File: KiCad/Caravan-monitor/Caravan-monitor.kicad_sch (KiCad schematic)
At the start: 24 parts, among them J1 Conn_ARM_JTAG_SWD_20, J2 8-28V input, SW2 SW_USER, SW3 SW_DPDT_x2, U2 STM32L010C6Tx

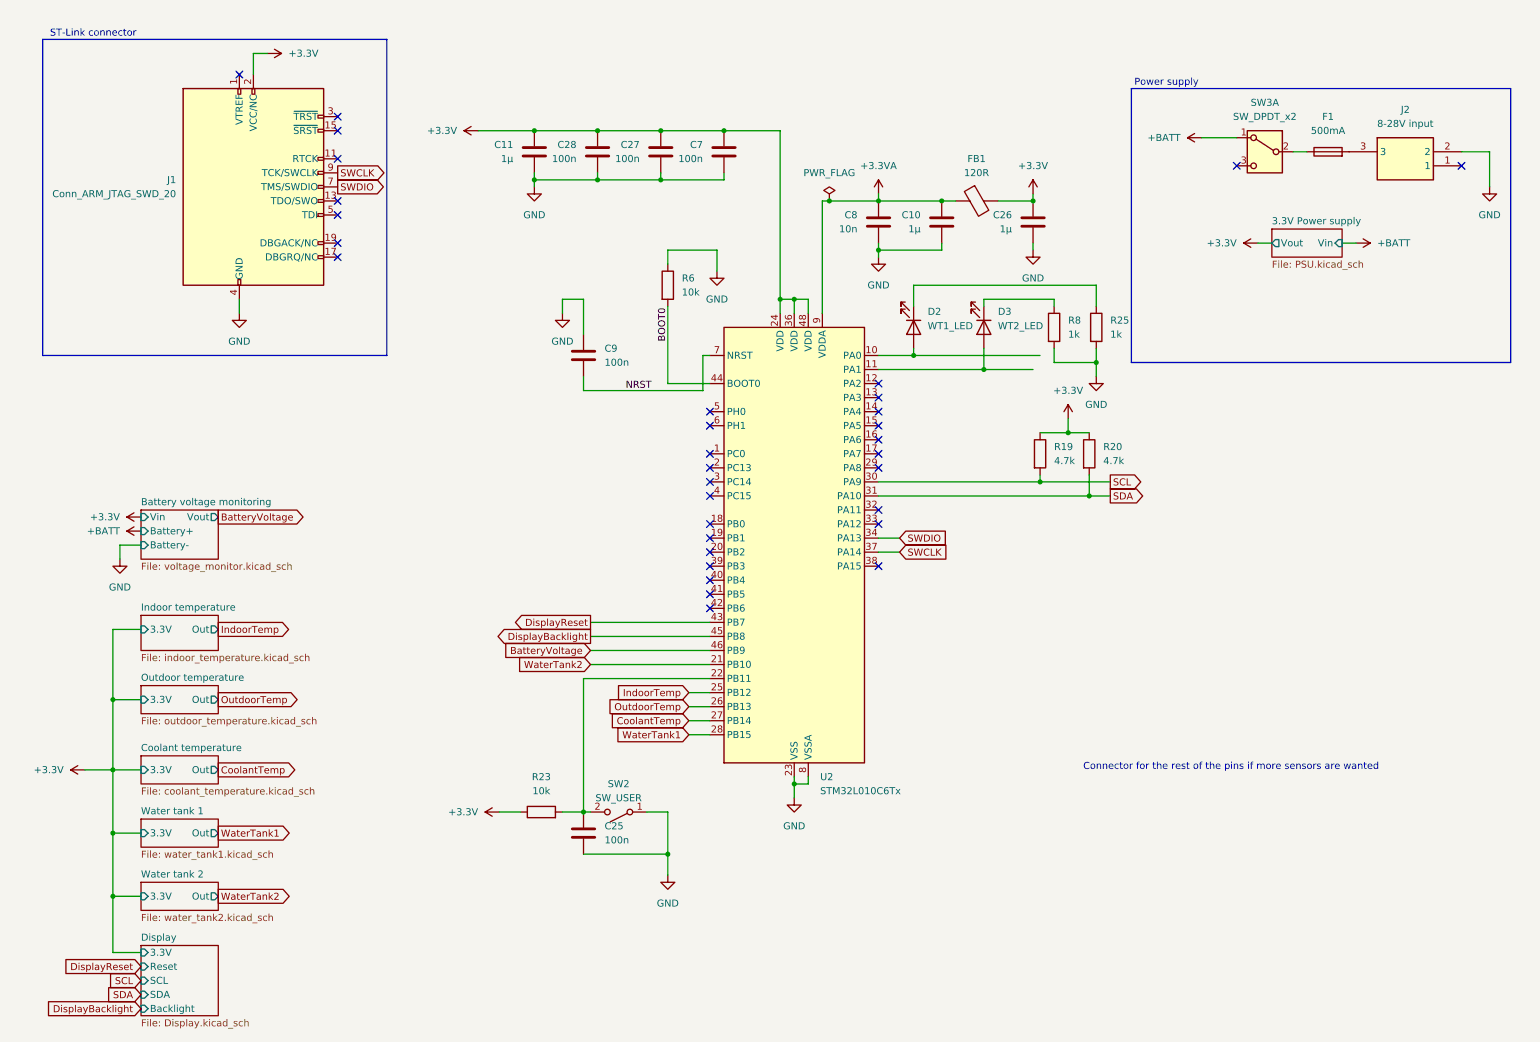
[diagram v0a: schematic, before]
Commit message: Schematic updates
Parts changed for JLCPCB assembly compatibility
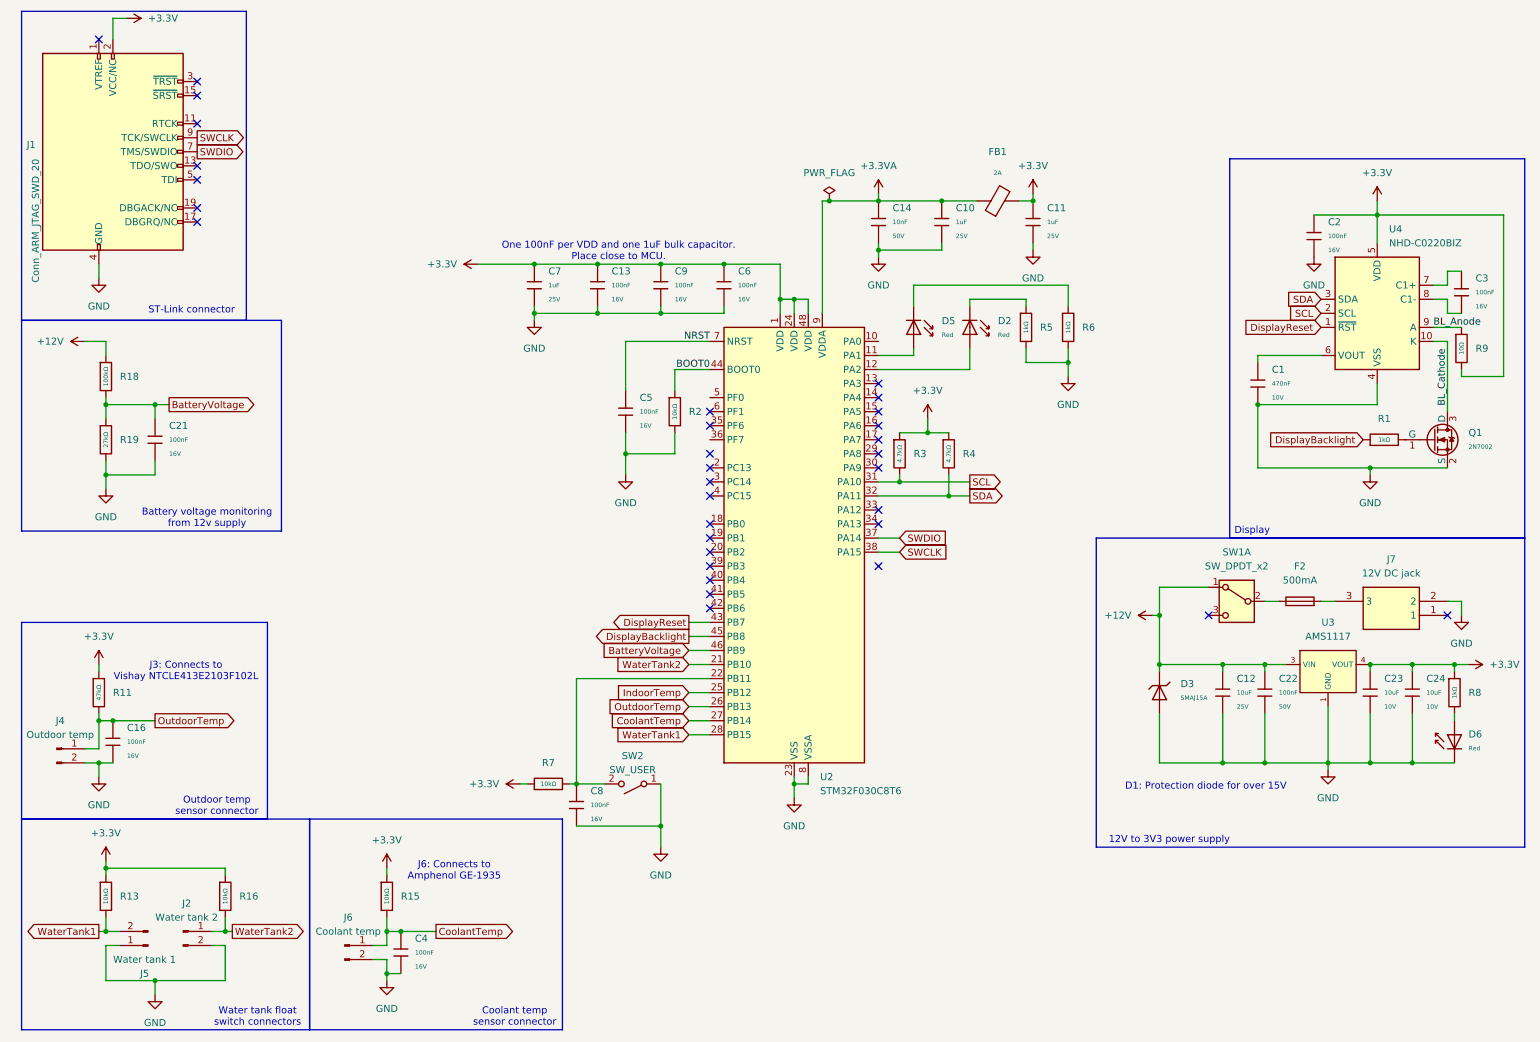
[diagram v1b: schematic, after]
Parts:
- removed C10, C11, C26: 1µ, Capacitor_SMD:C_0402_1005Metric_Pad0.74x0.62mm_HandSolder, symbol Device:C
- removed C25, C27, C28, C7, C9: 100n, Capacitor_SMD:C_0402_1005Metric_Pad0.74x0.62mm_HandSolder, symbol Device:C
- removed C8: 10n, Capacitor_SMD:C_0402_1005Metric_Pad0.74x0.62mm_HandSolder, symbol Device:C
- removed D2: WT1_LED, LED_SMD:LED_0402_1005Metric_Pad0.77x0.64mm_HandSolder, symbol Device:LED
- removed D3: WT2_LED, LED_SMD:LED_0402_1005Metric_Pad0.77x0.64mm_HandSolder, symbol Device:LED
- removed F1: 500mA, Fuse:Fuseholder_Clip-5x20mm_Littelfuse_111_Lateral_P18.80x5.00mm_D1.17mm_Horizontal, symbol Device:Fuse
- removed FB1: 120R, Inductor_SMD:L_0402_1005Metric_Pad0.77x0.64mm_HandSolder, symbol Device:FerriteBead
- removed J2: 8-28V input, SamacSys_Parts:PJ059A, symbol SamacSys_Parts:PJ-059A
- removed R19, R20: 4.7k, Resistor_SMD:R_0402_1005Metric_Pad0.72x0.64mm_HandSolder, symbol Device:R
- removed R23, R6: 10k, Resistor_SMD:R_0402_1005Metric_Pad0.72x0.64mm_HandSolder, symbol Device:R
- removed R25, R8: 1k, Resistor_SMD:R_0402_1005Metric_Pad0.72x0.64mm_HandSolder, symbol Device:R
- removed SW3: SW_DPDT_x2, Button_Switch_THT:SW_E-Switch_EG2219_DPDT_Angled, symbol Switch:SW_DPDT_x2
- removed U2: STM32L010C6Tx, Package_QFP:LQFP-48_7x7mm_P0.5mm, symbol MCU_ST_STM32L0:STM32L010C6Tx
- added C1: 470nF, PCM_JLCPCB:C_0402, symbol PCM_JLCPCB-Capacitors:0402,470nF
- added C10, C11, C7: 1uF, PCM_JLCPCB:C_0402, symbol PCM_JLCPCB-Capacitors:0402,1uF
- added C12: 10uF, PCM_JLCPCB:C_0805, symbol PCM_JLCPCB-Capacitors:0805,10uF
- added C13, C16, C2, C21, C3, C4, C5, C6, C8, C9: 100nF, PCM_JLCPCB:C_0402, symbol PCM_JLCPCB-Capacitors:0402,100nF
- added C14: 10nF, PCM_JLCPCB:C_0402, symbol PCM_JLCPCB-Capacitors:0402,10nF
- added C22: 100nF, PCM_JLCPCB:C_0603, symbol PCM_JLCPCB-Capacitors:0603,100nF
- added C23, C24: 10uF, PCM_JLCPCB:C_0603, symbol PCM_JLCPCB-Capacitors:0603,10uF
- added D2, D5, D6: Red, PCM_JLCPCB:D_0603, symbol PCM_JLCPCB-Diodes:LED,0603,Red
- added D3: SMAJ15A, PCM_JLCPCB:D_SMA, symbol PCM_JLCPCB-Diodes:TVS-Uni,SMAJ15A
- added F2: 500mA, Fuse:Fuseholder_Clip-5x20mm_Littelfuse_111_Lateral_P18.80x5.00mm_D1.17mm_Horizontal, symbol Device:Fuse
- added FB1: ~, PCM_JLCPCB:FB_0603, symbol PCM_JLCPCB-Inductors:Ferrite,0603,(2)
- added J2: Water tank 2, Connector_JST:JST_XH_S2B-XH-A-1_1x02_P2.50mm_Horizontal, symbol Connector:Conn_01x02_Pin
- added J4: Outdoor temp, Connector_JST:JST_XH_S2B-XH-A-1_1x02_P2.50mm_Horizontal, symbol Connector:Conn_01x02_Pin
- added J5: Water tank 1, Connector_JST:JST_XH_S2B-XH-A-1_1x02_P2.50mm_Horizontal, symbol Connector:Conn_01x02_Pin
- added J6: Coolant temp, Connector_JST:JST_XH_S2B-XH-A-1_1x02_P2.50mm_Horizontal, symbol Connector:Conn_01x02_Pin
- added J7: 12V DC jack, SamacSys_Parts:PJ059A, symbol SamacSys_Parts:PJ-059A
- added Q1: 2N7002, PCM_JLCPCB:Q_SOT-23, symbol PCM_JLCPCB-Transistors:NMOS,2N7002
- added R1, R5, R6, R8: 1kΩ, PCM_JLCPCB:R_0402, symbol PCM_JLCPCB-Resistors:0402,1kΩ
- added R11: 47kΩ, PCM_JLCPCB:R_0402, symbol PCM_JLCPCB-Resistors:0402,47kΩ
- added R13, R15, R16, R2, R7: 10kΩ, PCM_JLCPCB:R_0402, symbol PCM_JLCPCB-Resistors:0402,10kΩ
- added R18: 100kΩ, PCM_JLCPCB:R_0402, symbol PCM_JLCPCB-Resistors:0402,100kΩ
- added R19: 27kΩ, PCM_JLCPCB:R_0402, symbol PCM_JLCPCB-Resistors:0402,27kΩ
- added R3, R4: 4.7kΩ, PCM_JLCPCB:R_0402, symbol PCM_JLCPCB-Resistors:0402,4.7kΩ
- added R9: 10Ω, PCM_JLCPCB:R_0603, symbol PCM_JLCPCB-Resistors:0603,10Ω
- added SW1: SW_DPDT_x2, Button_Switch_THT:SW_E-Switch_EG2219_DPDT_Angled, symbol Switch:SW_DPDT_x2
- added U2: STM32F030C8T6, PCM_JLCPCB:LQFP-48_7x7mm_P0.5mm, symbol PCM_JLCPCB-MCUs:STM32F030C8T6
- added U3: AMS1117, PCM_JLCPCB:SOT-223-3_L6.5-W3.4-P2.30-LS7.0-BR, symbol PCM_JLCPCB-Power:LDO, 3.3V, 1A
- added U4: NHD-C0220BIZ, Display:NHD-C0220BiZ, symbol Display_Character:NHD-C0220BIZ
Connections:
- net +3.3V: now also C11.1, C13.1, C2.1, C23.1, C24.1, C6.1, C7.1, C9.1, FB1.2, R11.1, R13.1, R15.1, R16.1, R3.1, R4.1, R7.1, R8.1, R9.2, U2.1 (VDD), U2.24 (VDD), U2.48 (VDD), U3.2 (VOUT), U3.4 (VOUT), U4.5 (VDD)
- net +3.3VA: now also C10.1, C14.1, FB1.1, U2.9 (VDDA)
- net BOOT0: now also R2.1, U2.44 (BOOT0)
- net BatteryVoltage: now also C21.1, R18.2, R19.1, U2.46 (PB9)
- net CoolantTemp: now also C4.1, J6.1 (Pin_1), R15.2, U2.27 (PB14)
- net DisplayBacklight: now also R1.1, U2.45 (PB8)
- net DisplayReset: now also U2.43 (PB7), U4.1 (~{RST})
- net GND: now also C1.2, C10.2, C11.2, C12.2, C13.2, C14.2, C16.2, C2.2, C21.2, C22.2, C23.2, C24.2, C4.2, C5.2, C6.2, C7.2, C8.2, C9.2, D3.2, D6.1, J2.2 (Pin_2), J4.2 (Pin_2), J5.1 (Pin_1), J6.2 (Pin_2), J7.2, Q1.2 (S), R19.2, R2.2, R5.2, R6.2, U2.23 (VSS), U2.47 (VSS), U2.8 (VSSA), U3.1 (GND), U4.4 (VSS)
- net IndoorTemp: now also U2.25 (PB12)
- net NRST: now also C5.1, U2.7 (NRST)
- net OutdoorTemp: now also C16.1, J4.1 (Pin_1), R11.2, U2.26 (PB13)
- net SCL: now also R3.2, U2.31 (PA10), U4.2 (SCL)
- net SDA: now also R4.2, U2.32 (PA11), U4.3 (SDA)
- net SWCLK: now also U2.38 (PA15)
- net SWDIO: now also U2.37 (PA14)
- net WaterTank1: now also J5.2 (Pin_2), R13.2, U2.28 (PB15)
- net WaterTank2: now also J2.1 (Pin_1), R16.2, U2.21 (PB10)
- net at SW2.2 (B): now also C8.1, R7.2, U2.22 (PB11)
- new net: F2.1, SW1.2 (B)
- new net: D5.2, U2.11 (PA1)
- new net: D2.2, U2.12 (PA2)
- new net: D2.1, R5.1
- new net: C1.1, U4.6 (VOUT)
- new net: C3.1, U4.7 (C1+)
- new net: C3.2, U4.8 (C1-)
- new net: D5.1, R6.1
- new net: F2.2, J7.3
- new net: Q1.1 (G), R1.2
- new net: D6.2, R8.2
- new net +12V: C12.1, C22.1, D3.1, R18.1, SW1.1 (A), U3.3 (VIN)
- new net BL_Anode: R9.1, U4.9 (A)
- new net BL_Cathode: Q1.3 (D), U4.10 (K)
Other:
- removed sheet 3.3V Power supply
- removed sheet Battery voltage monitoring
- removed sheet Coolant temperature
- removed sheet Display
- removed sheet Indoor temperature
- removed sheet Outdoor temperature
- removed sheet Water tank 1
- removed sheet Water tank 2
- note added: "12V to 3V3 power supply"
- note added: "Battery voltage monitoring from 12v supply"
- note added: "Coolant temp sensor connector"
- note added: "D1: Protection diode for over 15V"
- note added: "Display"
- note added: "J3: Connects to Vishay NTCLE413E2103F102L"
- note added: "J6: Connects to Amphenol GE-1935"
- note added: "One 100nF per VDD and one 1uF bulk capacitor. Place close to MCU."
- note added: "Outdoor temp sensor connector"
- note added: "Water tank float switch connectors"
- note removed: "Connector for the rest of the pins if more sensors are wanted"
- note removed: "Power supply"
- moved on the sheet: J1, SW2

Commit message: 12V to 3.3V converter done
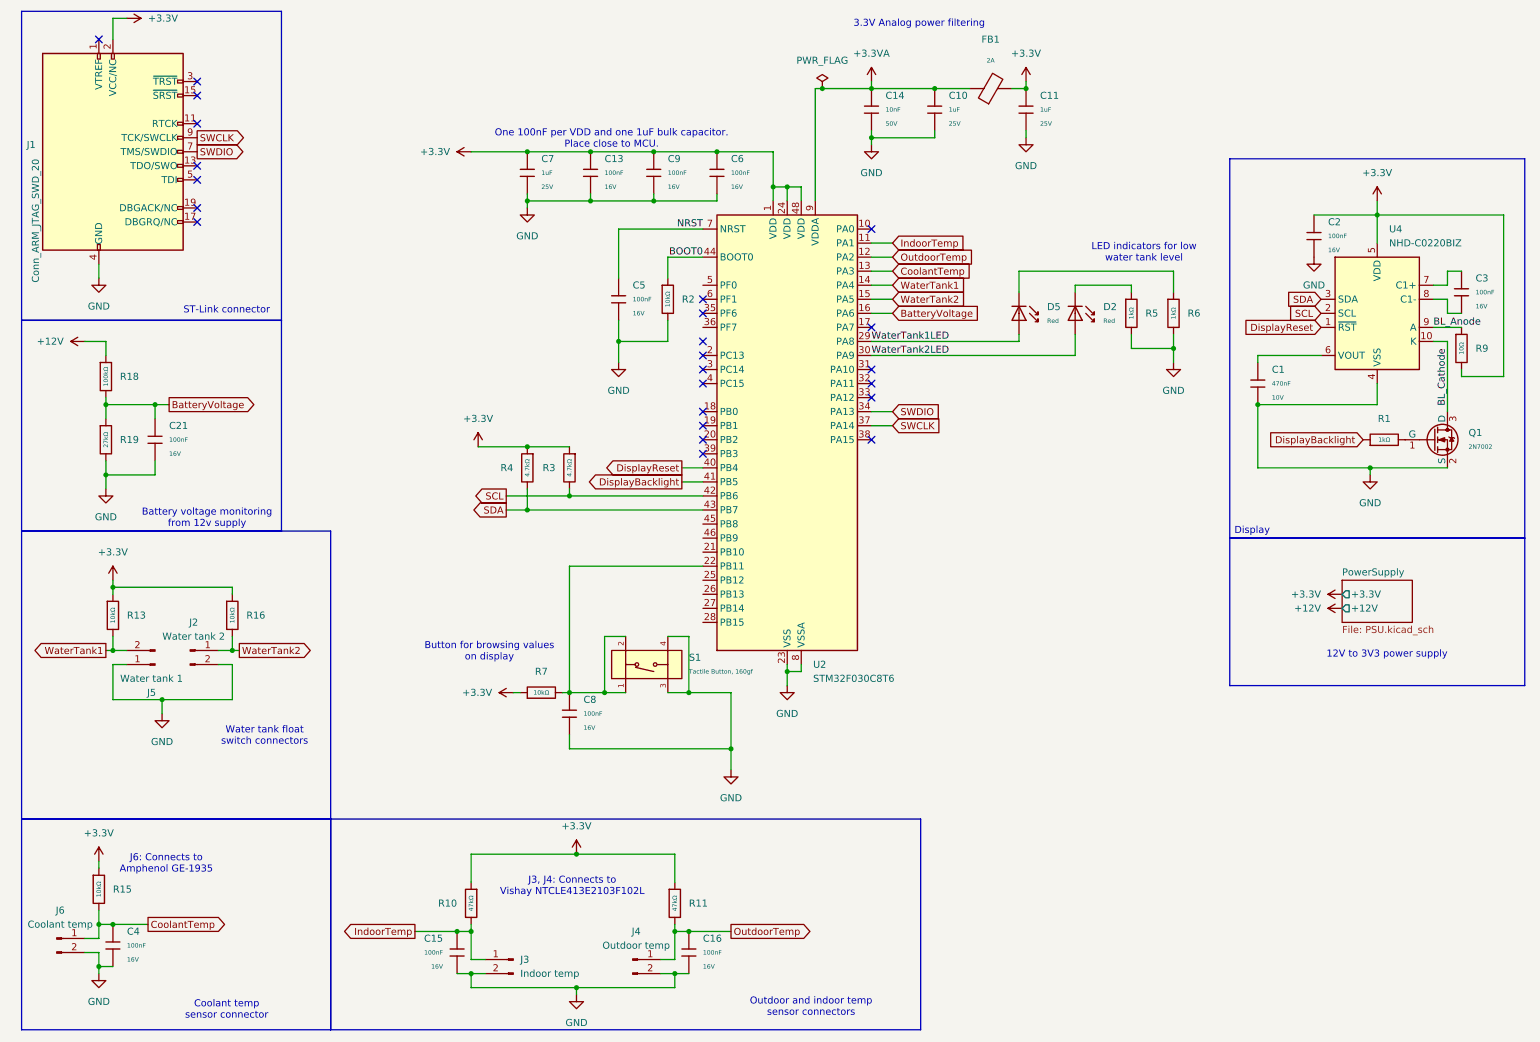
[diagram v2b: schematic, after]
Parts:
- removed C12: 10uF, PCM_JLCPCB:C_0805, symbol PCM_JLCPCB-Capacitors:0805,10uF
- removed C22: 100nF, PCM_JLCPCB:C_0603, symbol PCM_JLCPCB-Capacitors:0603,100nF
- removed C23, C24: 10uF, PCM_JLCPCB:C_0603, symbol PCM_JLCPCB-Capacitors:0603,10uF
- removed D3: SMAJ15A, PCM_JLCPCB:D_SMA, symbol PCM_JLCPCB-Diodes:TVS-Uni,SMAJ15A
- removed D6: Red, PCM_JLCPCB:D_0603, symbol PCM_JLCPCB-Diodes:LED,0603,Red
- removed F2: 500mA, Fuse:Fuseholder_Clip-5x20mm_Littelfuse_111_Lateral_P18.80x5.00mm_D1.17mm_Horizontal, symbol Device:Fuse
- removed J7: 12V DC jack, SamacSys_Parts:PJ059A, symbol SamacSys_Parts:PJ-059A
- removed R8: 1kΩ, PCM_JLCPCB:R_0402, symbol PCM_JLCPCB-Resistors:0402,1kΩ
- removed SW1: SW_DPDT_x2, Button_Switch_THT:SW_E-Switch_EG2219_DPDT_Angled, symbol Switch:SW_DPDT_x2
- removed SW2: SW_USER, Button_Switch_SMD:SW_SPST_PTS645, symbol Switch:SW_SPST
- removed U3: AMS1117, PCM_JLCPCB:SOT-223-3_L6.5-W3.4-P2.30-LS7.0-BR, symbol PCM_JLCPCB-Power:LDO, 3.3V, 1A
- added C15: 100nF, PCM_JLCPCB:C_0402, symbol PCM_JLCPCB-Capacitors:0402,100nF
- added J3: Indoor temp, Connector_JST:JST_XH_S2B-XH-A-1_1x02_P2.50mm_Horizontal, symbol Connector:Conn_01x02_Pin
- added R10: 47kΩ, PCM_JLCPCB:R_0402, symbol PCM_JLCPCB-Resistors:0402,47kΩ
- added S1: Tactile Button, 160gf, PCM_JLCPCB:SW-SMD_4P-L5.1-W5.1-P3.70-LS6.5-TL-2, symbol PCM_JLCPCB-Connectors_Buttons:Tactile Button, 160gf, 12V, 50mA, 5.1mm
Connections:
- net +3.3V: now also R10.1
- net BatteryVoltage: now also U2.16 (PA6); no longer U2.46 (PB9)
- net CoolantTemp: now also U2.13 (PA3); no longer U2.27 (PB14)
- net DisplayBacklight: now also U2.41 (PB5); no longer U2.45 (PB8)
- net DisplayReset: now also U2.40 (PB4); no longer U2.43 (PB7)
- net GND: now also C15.2, J3.2 (Pin_2), S1.3 (C), S1.4 (D)
- net IndoorTemp: now also U2.11 (PA1), C15.1, J3.1 (Pin_1), R10.2; no longer U2.25 (PB12)
- net OutdoorTemp: now also U2.12 (PA2); no longer U2.26 (PB13)
- net SCL: now also U2.42 (PB6); no longer U2.31 (PA10)
- net SDA: now also U2.43 (PB7); no longer U2.32 (PA11)
- net SWCLK: now also U2.37 (PA14); no longer U2.38 (PA15)
- net SWDIO: now also U2.34 (PA13); no longer U2.37 (PA14)
- net WaterTank1: now also U2.14 (PA4); no longer U2.28 (PB15)
- net WaterTank2: now also U2.15 (PA5); no longer U2.21 (PB10)
- net WaterTank1LED: now reaches D5.2
- net WaterTank1LED: now also U2.29 (PA8); no longer U2.11 (PA1)
- net WaterTank2LED: now reaches D2.2
- net WaterTank2LED: now also U2.30 (PA9); no longer U2.12 (PA2)
- net at C8.1, R7.2, U2.22 (PB11): now also S1.1 (A), S1.2 (B)
- no-connect marks 33 -> 24
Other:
- added sheet PowerSupply (PSU.kicad_sch)
- note added: "3.3V Analog power filtering"
- note added: "Button for browsing values on display"
- note added: "J3, J4: Connects to Vishay NTCLE413E2103F102L"
- note added: "LED indicators for low water tank level"
- note added: "Outdoor and indoor temp sensor connectors"
- note removed: "D1: Protection diode for over 15V"
- note removed: "J3: Connects to Vishay NTCLE413E2103F102L"
- note removed: "Outdoor temp sensor connector"
- moved on the sheet: C10, C11, C13, C14, C16, C4, C5, C6, C7, C8, C9, D2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

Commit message: V0.2 PCB complete
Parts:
- removed C1: 470nF, PCM_JLCPCB:C_0402, symbol PCM_JLCPCB-Capacitors:0402,470nF
- removed C3: 100nF, PCM_JLCPCB:C_0402, symbol PCM_JLCPCB-Capacitors:0402,100nF
- removed J1: Conn_ARM_JTAG_SWD_20, Connector_IDC:IDC-Header_2x10_P2.54mm_Horizontal, symbol Connector:Conn_ARM_JTAG_SWD_20
- removed J2: Water tank 2, Connector_JST:JST_XH_S2B-XH-A-1_1x02_P2.50mm_Horizontal, symbol Connector:Conn_01x02_Pin
- removed J3: Indoor temp, Connector_JST:JST_XH_S2B-XH-A-1_1x02_P2.50mm_Horizontal, symbol Connector:Conn_01x02_Pin
- removed J4: Outdoor temp, Connector_JST:JST_XH_S2B-XH-A-1_1x02_P2.50mm_Horizontal, symbol Connector:Conn_01x02_Pin
- removed J5: Water tank 1, Connector_JST:JST_XH_S2B-XH-A-1_1x02_P2.50mm_Horizontal, symbol Connector:Conn_01x02_Pin
- removed J6: Coolant temp, Connector_JST:JST_XH_S2B-XH-A-1_1x02_P2.50mm_Horizontal, symbol Connector:Conn_01x02_Pin
- removed Q1: 2N7002, PCM_JLCPCB:Q_SOT-23, symbol PCM_JLCPCB-Transistors:NMOS,2N7002
- removed R1: 1kΩ, PCM_JLCPCB:R_0402, symbol PCM_JLCPCB-Resistors:0402,1kΩ
- removed R9: 10Ω, PCM_JLCPCB:R_0603, symbol PCM_JLCPCB-Resistors:0603,10Ω
- removed U4: NHD-C0220BIZ, Display:NHD-C0220BiZ, symbol Display_Character:NHD-C0220BIZ
- added C1: 100nF, PCM_JLCPCB:C_0402, symbol PCM_JLCPCB-Capacitors:0402,100nF
- added C19, C20: 12pF, PCM_JLCPCB:C_0402, symbol PCM_JLCPCB-Capacitors:0402,12pF
- added CN2: HX JN1.27-2X7P ZZ H4.9, EasyEDA:IDC-TH_14P-P1.27_C42455940, symbol EasyEDA:HXJN1.27-2X7PZZH4.9
- added R12: 0Ω, PCM_JLCPCB:R_0402, symbol PCM_JLCPCB-Resistors:0402,0Ω
- added S2: Tactile Button, 160gf, PCM_JLCPCB:SW-SMD_4P-L5.1-W5.1-P3.70-LS6.5-TL-2, symbol PCM_JLCPCB-Connectors_Buttons:Tactile Button, 160gf, 12V, 50mA, 5.1mm
- added U1, U5, U6, U7, U8: S2B-PH-K-S, EasyEDA:CONN-TH_S2B-PH-K-S-LF-SN, symbol EasyEDA:S2B-PH-K-S
- added U4: HS96L03W2C03, EasyEDA:OLED-TH_L27.8-W27.2-P2.54_C9900033791, symbol EasyEDA:HS96L03W2C03
- added X1: X322516MLB4SI, PCM_JLCPCB:OSC-SMD_4P-L3.2-W2.5-BL, symbol PCM_JLCPCB-Crystals:Crystal, 16MHz, 9pF
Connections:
- net +3.3V: now also CN2.3, U4.2 (VCC); no longer C2.1
- net CoolantTemp: now also U6.1
- net GND: now also C1.2, C19.1, C20.1, CN2.11, CN2.5, CN2.7, S2.1 (A), S2.2 (B), U1.2, U4.1 (GND), U5.2, U6.2, U7.2, U8.2, X1.2 (GND), X1.4 (GND)
- net IndoorTemp: now also U7.1
- net NRST: now also CN2.12, S2.3 (C), S2.4 (D)
- net OutdoorTemp: now also U8.1
- net SCL: now also U4.3 (SCL)
- net SDA: now also U4.4 (SDA)
- net SWCLK: now also CN2.6
- net SWDIO: now also CN2.4
- net WaterTank1: now also C2.1, U1.1
- net WaterTank2: now also C1.1, U5.1
- net at U2.5 (PF0): now also C19.2, X1.1 (OSC)
- net at U2.6 (PF1): now also R12.2
- net DisplayBacklight: no longer names the net of U2.41 (PB5)
- net DisplayReset: no longer names the net of U2.40 (PB4)
- new net: C20.2, R12.1, X1.3 (OSC)
- no-connect marks 24 -> 32
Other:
- note added: "Water tank float sensor connectors"
- note removed: "Water tank float switch connectors"
- moved on the sheet: C5, R16, R2
